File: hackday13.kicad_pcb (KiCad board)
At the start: 2 copper layers, 0 parts

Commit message: Incomplete attempt at PCB
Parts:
- added BT1: 3V, Battery:BatteryHolder_Keystone_3002_1x2032, F.Cu at (200.8, 137.0)
- added D1: D_Schottky, Diode_THT:D_DO-35_SOD27_P7.62mm_Horizontal, F.Cu at (79.8, 120.0)
- added D4: D_Schottky, Diode_THT:D_DO-35_SOD27_P7.62mm_Horizontal, F.Cu at (157.2, 131.0)
- added J1: TT-output, TinyTapeout:PinHeader_2x06_P2.54mm_PMODPeriph2B, F.Cu at (146.5, 39.5)
- added J2: TT-input, TinyTapeout:PinHeader_2x06_P2.54mm_PMODPeriph2B, F.Cu at (100.7, 39.6)
- added J3: TT-bidirectional, TinyTapeout:PinHeader_2x06_P2.54mm_PMODPeriph2B, F.Cu at (122.7, 39.6)
- added LEDs1: LED dot matrix 12 pin, custom_components_led_pcb:LED_dot_matrix_TA07-11SEKWA, F.Cu at (216.4, 54.0)
- added R1: 200 Ohm, Resistor_THT:R_Axial_DIN0207_L6.3mm_D2.5mm_P10.16mm_Horizontal, F.Cu at (202.1, 53.0)
- added R2: 200 Ohm, Resistor_THT:R_Axial_DIN0207_L6.3mm_D2.5mm_P10.16mm_Horizontal, F.Cu at (198.2, 64.0)
- added R3: 200 Ohm, Resistor_THT:R_Axial_DIN0207_L6.3mm_D2.5mm_P10.16mm_Horizontal, F.Cu at (263.0, 76.9)
- added R4: 200 Ohm, Resistor_THT:R_Axial_DIN0207_L6.3mm_D2.5mm_P10.16mm_Horizontal, F.Cu at (239.0, 76.9)
- added R5: 200 Ohm, Resistor_THT:R_Axial_DIN0207_L6.3mm_D2.5mm_P10.16mm_Horizontal, F.Cu at (251.0, 76.9)
- added SW1: Reset button, Button_Switch_THT:SW_PUSH_6mm, F.Cu at (62.8, 82.8)
- added SW2: SW_DIP_x02, Button_Switch_THT:SW_DIP_SPSTx02_Slide_9.78x7.26mm_W7.62mm_P2.54mm, F.Cu at (95.2, 135.7)
- added ShReg1: MC14014B, Package_SO:SOIC-16_3.9x9.9mm_P1.27mm, F.Cu at (128.8, 56.5)
- added ShReg2: MC14014B, Package_SO:SOIC-16_3.9x9.9mm_P1.27mm, F.Cu at (151.5, 57.0)
- added ShReg3: 74HC595, Package_SO:SOIC-16_3.9x9.9mm_P1.27mm, F.Cu at (102.8, 56.5)
- added U1: RaspberryPi_Pico, Module_RaspberryPi_Pico:RaspberryPi_Pico_Common, F.Cu at (124.0, 95.0)
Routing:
- net VCC: track 0.00 -> 293.9 mm
- net Net-(LEDs1-R1): track 0.00 -> 219.9 mm
- net Net-(U1-GPIO16): track 0.00 -> 178.3 mm
- net Net-(D1-K): track 0.00 -> 139.2 mm
- net GND: track 0.00 -> 102.8 mm
- net Net-(U1-GPIO12): track 0.00 -> 96.3 mm
- net Net-(U1-GPIO13): track 0.00 -> 84.8 mm
- net Net-(BT1-+): track 0.00 -> 60.6 mm
- net Net-(J3-IO2): track 0.00 -> 48.9 mm
- net Net-(LEDs1-C3): track 0.00 -> 46.4 mm
- net Net-(U1-GPIO28_ADC2): track 0.00 -> 44.3 mm
- net Net-(J3-IO1): track 0.00 -> 37.9 mm
- net Net-(LEDs1-C5): track 0.00 -> 32.3 mm
- net Net-(J2-IO5): track 0.00 -> 26.8 mm
- net Net-(J1-IO2): track 0.00 -> 26.0 mm
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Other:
- board outline added: 235 x 128 mm

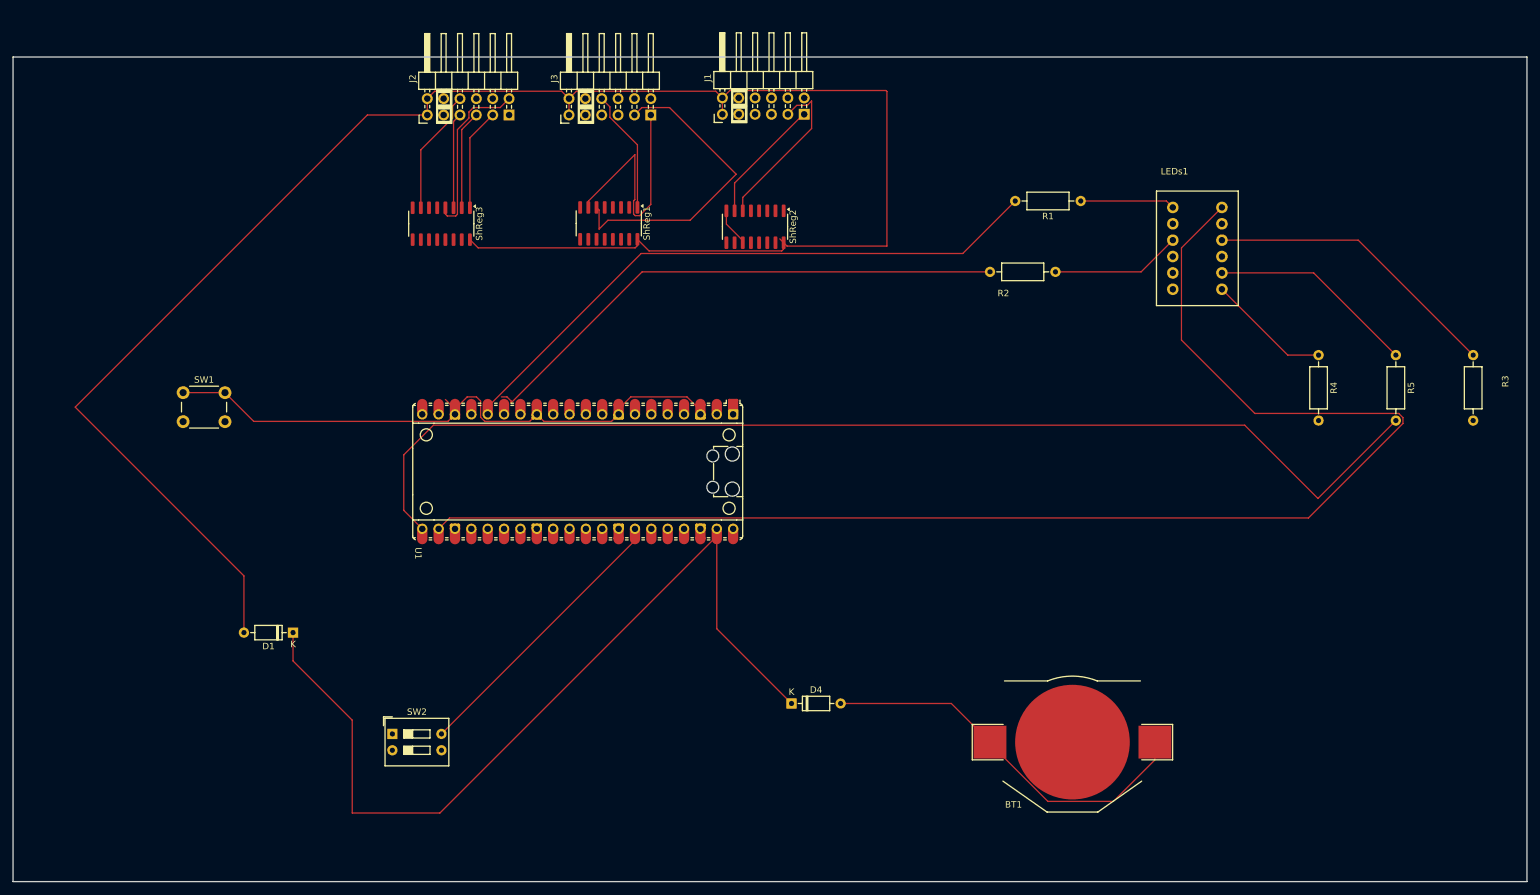
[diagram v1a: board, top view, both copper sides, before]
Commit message: Make PCB more compact and remove more ground lines
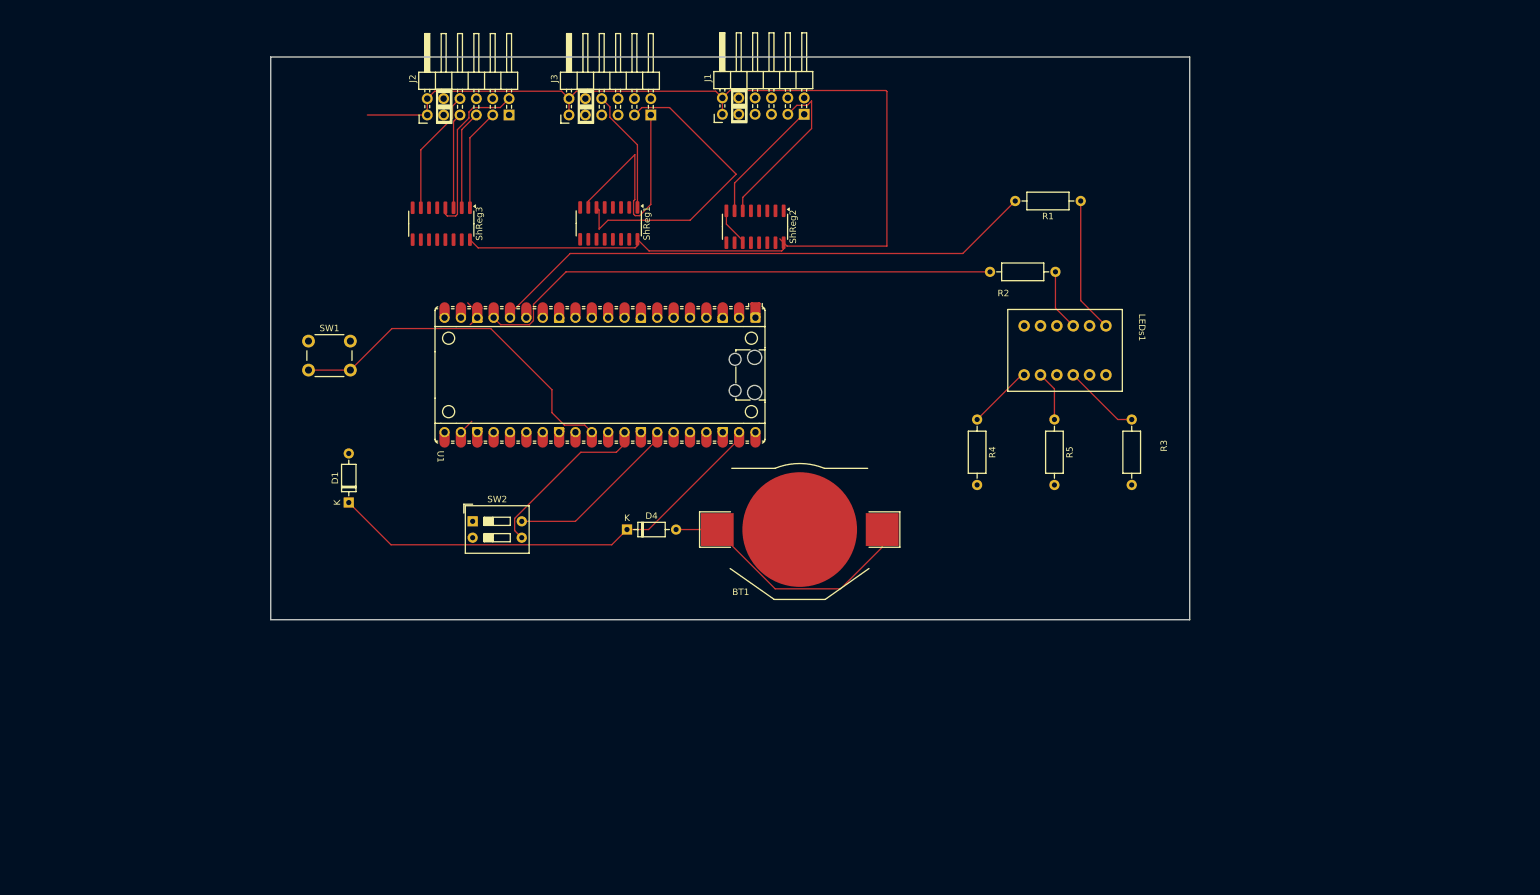
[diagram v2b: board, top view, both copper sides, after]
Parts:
- moved R3 53.9 mm to (210.0, 86.9)
- moved R4 53.9 mm to (186.0, 86.9)
- moved R5 53.9 mm to (198.0, 86.9)
- moved BT1 53.7 mm to (158.5, 104.0)
- moved D4 37.2 mm to (131.7, 104.0)
- moved SW2 35.3 mm to (107.7, 102.7)
- moved D1 22.0 mm to (88.5, 99.8), turned to 90 degrees
- moved LEDs1 21.1 mm to (206.0, 72.4), turned to -90 degrees
- moved SW1 21.0 mm to (82.2, 74.8)
- moved U1 15.4 mm to (127.5, 80.0)
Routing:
- net Net-(LEDs1-R1): track 219.9 -> 2.39 mm
- net Net-(U1-GPIO16): track 178.3 -> 0.00 mm
- net VCC: track 293.9 -> 184.0 mm
- net GND: track 102.8 -> 14.9 mm
- net Net-(D1-K): track 139.2 -> 72.3 mm
- net Net-(U1-RUN): track 0.00 -> 55.4 mm
- net Net-(LEDs1-C3): track 46.4 -> 11.9 mm
- net Net-(U1-GPIO27_ADC1): track 0.00 -> 27.1 mm
- net Net-(LEDs1-C5): track 32.3 -> 7.81 mm
- net Net-(BT1-+): track 60.6 -> 41.3 mm
- net Net-(U1-GPIO28_ADC2): track 44.3 -> 29.2 mm
- net Net-(LEDs1-C2): track 20.3 -> 9.52 mm
- net Net-(LEDs1-C4): track 19.2 -> 10.2 mm
- net Net-(U1-GPIO12): track 96.3 -> 87.4 mm
- net Net-(LEDs1-C1): track 14.7 -> 21.0 mm
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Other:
- board size 235 x 128 mm -> 142.7 x 87.3 mm

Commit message: [layout] Start with new 4-L layout
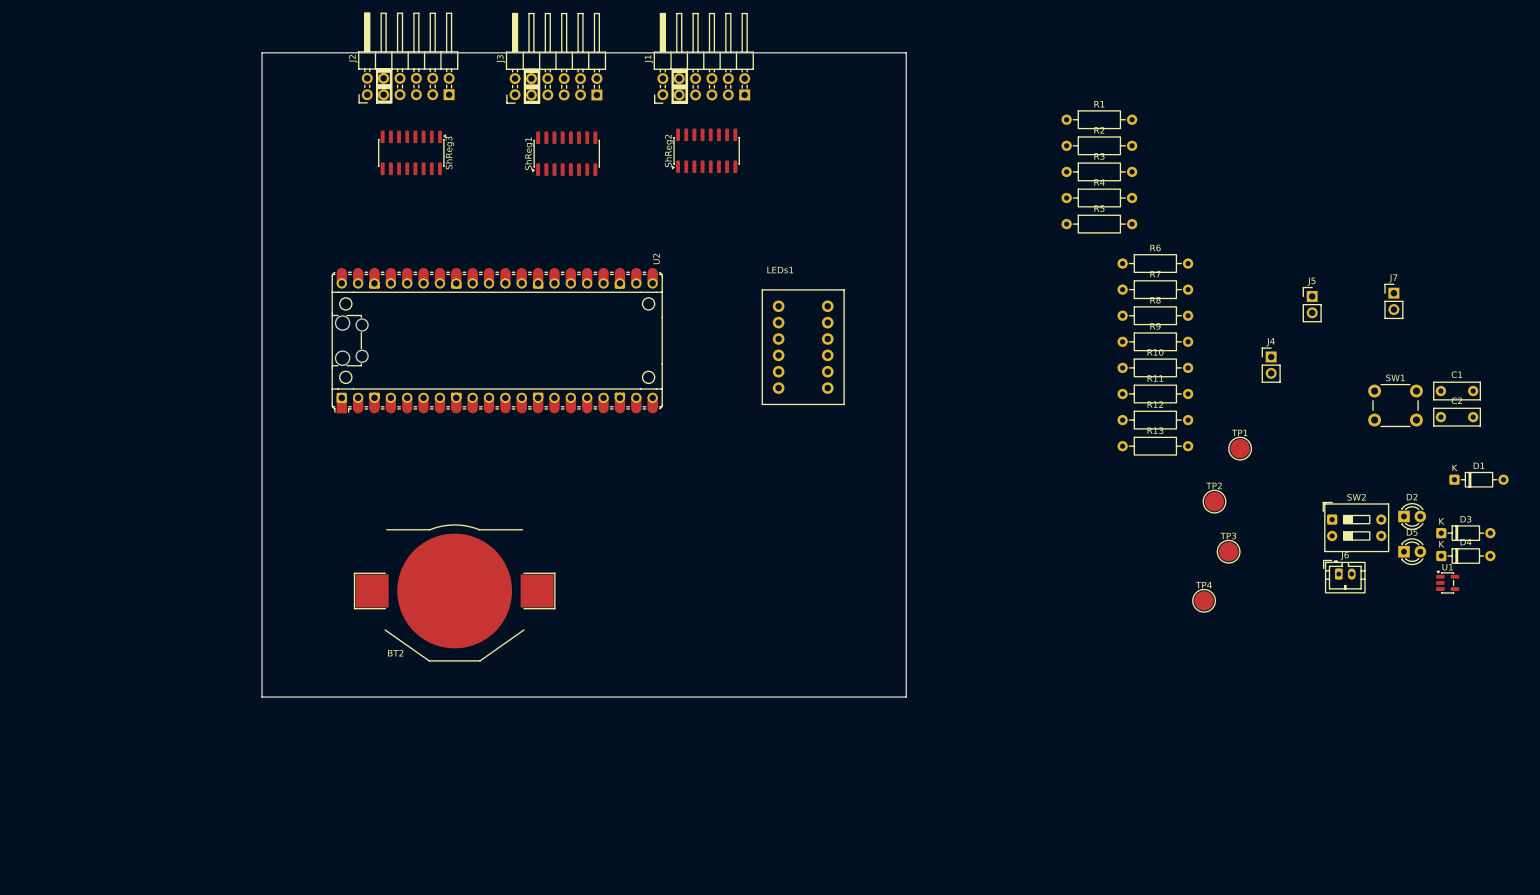
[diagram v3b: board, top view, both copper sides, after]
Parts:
- removed BT1: 3V, Battery:BatteryHolder_Keystone_3002_1x2032
- added BT2: Battery_Cell, Battery:BatteryHolder_Keystone_3002_1x2032, F.Cu at (104.9, 113.5)
- added C1: 4.7u, Capacitor_THT:C_Disc_D7.0mm_W2.5mm_P5.00mm, F.Cu at (258.0, 82.5)
- added C2: 4.7u, Capacitor_THT:C_Disc_D7.0mm_W2.5mm_P5.00mm, F.Cu at (258.0, 86.5)
- added D2: LED, LED_THT:LED_D3.0mm, F.Cu at (252.3, 102.0)
- added D3: D_Schottky, Diode_THT:D_DO-35_SOD27_P7.62mm_Horizontal, F.Cu at (258.1, 104.6)
- added D5: LED, LED_THT:LED_D3.0mm, F.Cu at (252.3, 107.4)
- added J4: Conn_01x02_Pin, Connector_PinHeader_2.54mm:PinHeader_1x02_P2.54mm_Vertical, F.Cu at (231.6, 77.2)
- added J5: Conn_01x02_Pin, Connector_PinHeader_2.54mm:PinHeader_1x02_P2.54mm_Vertical, F.Cu at (238.0, 67.8)
- added J6: Conn_01x02_Pin, Connector_JST:JST_PH_B2B-PH-K_1x02_P2.00mm_Vertical, F.Cu at (242.2, 110.9)
- added J7: Conn_01x02_Pin, Connector_PinHeader_2.54mm:PinHeader_1x02_P2.54mm_Vertical, F.Cu at (250.7, 67.3)
- added R10: 1k, Resistor_THT:R_Axial_DIN0207_L6.3mm_D2.5mm_P10.16mm_Horizontal, F.Cu at (208.6, 78.9)
- added R11: 0, Resistor_THT:R_Axial_DIN0207_L6.3mm_D2.5mm_P10.16mm_Horizontal, F.Cu at (208.6, 83.0)
- added R12: 0, Resistor_THT:R_Axial_DIN0207_L6.3mm_D2.5mm_P10.16mm_Horizontal, F.Cu at (208.6, 87.0)
- added R13: 1000 Ohm, Resistor_THT:R_Axial_DIN0207_L6.3mm_D2.5mm_P10.16mm_Horizontal, F.Cu at (208.6, 91.1)
- added R6: 2k, Resistor_THT:R_Axial_DIN0207_L6.3mm_D2.5mm_P10.16mm_Horizontal, F.Cu at (208.6, 62.7)
- added R7: 1000 Ohm, Resistor_THT:R_Axial_DIN0207_L6.3mm_D2.5mm_P10.16mm_Horizontal, F.Cu at (208.6, 66.8)
- added R8: 1k, Resistor_THT:R_Axial_DIN0207_L6.3mm_D2.5mm_P10.16mm_Horizontal, F.Cu at (208.6, 70.8)
- added R9: 1k, Resistor_THT:R_Axial_DIN0207_L6.3mm_D2.5mm_P10.16mm_Horizontal, F.Cu at (208.6, 74.9)
- added TP1: TestPoint, TestPoint:TestPoint_Pad_D3.0mm, F.Cu at (226.8, 91.4)
- added TP2: TestPoint, TestPoint:TestPoint_Pad_D3.0mm, F.Cu at (222.8, 99.7)
- added TP3: TestPoint, TestPoint:TestPoint_Pad_D3.0mm, F.Cu at (225.0, 107.4)
- added TP4: TestPoint, TestPoint:TestPoint_Pad_D3.0mm, F.Cu at (221.2, 115.1)
- added U2: RaspberryPi_Pico_W, Module_RaspberryPi_Pico:RaspberryPi_Pico_Common, F.Cu at (111.5, 74.7)
- LEDs1: value LED dot matrix 12 pin -> LED dot matrix 12 pin
- U1: value RaspberryPi_Pico -> MCP73831-4-OT; footprint Module_RaspberryPi_Pico:RaspberryPi_Pico_Common -> Package_TO_SOT_SMD:SOT-23-5
- moved D1 171.7 mm to (260.1, 96.3), turned to 0 degrees
- moved SW1 165.7 mm to (247.7, 82.5)
- moved U1 135.5 mm to (259.1, 112.3), turned to 0 degrees
- moved SW2 133.4 mm to (241.1, 102.5)
- moved D4 126.5 mm to (258.1, 108.1)
- moved LEDs1 50.9 mm to (155.2, 69.3), turned to 0 degrees
- moved R3 39.7 mm to (199.9, 48.5), turned to 0 degrees
- moved R4 37.1 mm to (199.9, 52.5), turned to 0 degrees
- moved R5 30.4 mm to (199.9, 56.6), turned to 0 degrees
- moved R2 19.6 mm to (199.9, 44.4), turned to 0 degrees
- moved ShReg2 14.0 mm to (144.0, 45.2), turned to 90 degrees
- moved R1 12.8 mm to (199.9, 40.4), turned to 0 degrees
- moved ShReg1 12.6 mm to (122.3, 45.7), turned to 90 degrees
- moved ShReg3 11.9 mm to (98.2, 45.5)
- moved J2 9.83 mm to (91.3, 36.5)
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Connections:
- D1 pad 1: Net-(D1-K) -> +BATT
- D4 pad 1: Net-(D1-K) -> +BATT
- D4 pad 2: Net-(BT1-+) -> /Bat_Chg
- LEDs1 pad 11: Net-(LEDs1-R2) -> /DotMat_R2
- LEDs1 pad 12: Net-(LEDs1-R1) -> /DotMat_R1
- LEDs1 pad 2: Net-(LEDs1-R3) -> /DotMat_R3
- LEDs1 pad 4: Net-(LEDs1-R5) -> /DotMat_R5
- LEDs1 pad 5: Net-(LEDs1-R6) -> /DotMat_R6
- LEDs1 pad 6: Net-(LEDs1-R7) -> /DotMat_R7
- LEDs1 pad 9: Net-(LEDs1-R4) -> /DotMat_R4
- R1 pad 2: Net-(U1-GPIO12) -> Net-(U2-GPIO12)
- R2 pad 2: Net-(U1-GPIO13) -> Net-(U2-GPIO13)
- R3 pad 2: Net-(U1-GPIO14) -> Net-(U2-GPIO14)
- R4 pad 2: Net-(U1-GPIO15) -> Net-(U2-GPIO15)
- R5 pad 2: Net-(U1-GPIO16) -> Net-(U2-GPIO16)
- SW1 pad 2: Net-(U1-RUN) -> Net-(U2-RUN)
- SW2 pad 3: Net-(U1-GPIO27_ADC1) -> Net-(U2-GPIO27_ADC1)
- SW2 pad 4: Net-(U1-GPIO28_ADC2) -> Net-(U2-GPIO28_ADC2)
- ShReg2 pad 12: unconnected-(ShReg2-Q7-Pad12) -> Net-(ShReg2-Q7)
- ShReg3 pad 10: GND -> Net-(ShReg3-~{SRCLR})
- ShReg3 pad 13: GND -> Net-(ShReg3-~{OE})
- U1 pad 1: Net-(ShReg3-RCLK) -> /charge_ind
- U1 pad 2: Net-(ShReg3-SRCLK) -> GND
- U1 pad 3: GND -> /Bat_Chg
- U1 pad 4: Net-(ShReg3-SER) -> +5V
- U1 pad 5: Net-(ShReg2-Q8) -> Net-(U1-PROG)
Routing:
- net VCC: track 184.0 -> 0.00 mm
- net Net-(U1-GPIO12): track 87.4 -> 0.00 mm
- net Net-(U1-GPIO13): track 82.4 -> 0.00 mm
- net Net-(D1-K): track 72.3 -> 0.00 mm
- net Net-(U1-RUN): track 55.4 -> 0.00 mm
- net Net-(J3-IO2): track 48.9 -> 0.00 mm
- net Net-(BT1-+): track 41.3 -> 0.00 mm
- net Net-(J3-IO1): track 37.9 -> 0.00 mm
- net Net-(U1-GPIO28_ADC2): track 29.2 -> 0.00 mm
- net Net-(U1-GPIO27_ADC1): track 27.1 -> 0.00 mm
- net Net-(J2-IO5): track 26.8 -> 0.00 mm
- net Net-(J1-IO2): track 26.0 -> 0.00 mm
- net Net-(LEDs1-C1): track 21.0 -> 0.00 mm
- net Net-(J1-IO1): track 19.5 -> 0.00 mm
- net Net-(J2-IO8): track 19.5 -> 0.00 mm
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- added copper zone on In2.Cu, net GND
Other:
- board size 142.7 x 87.3 mm -> 100 x 100 mm
- copper layers 2 -> 4
